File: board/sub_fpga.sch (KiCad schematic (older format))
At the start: 3 parts, among them U201 XC3S200-TQ144

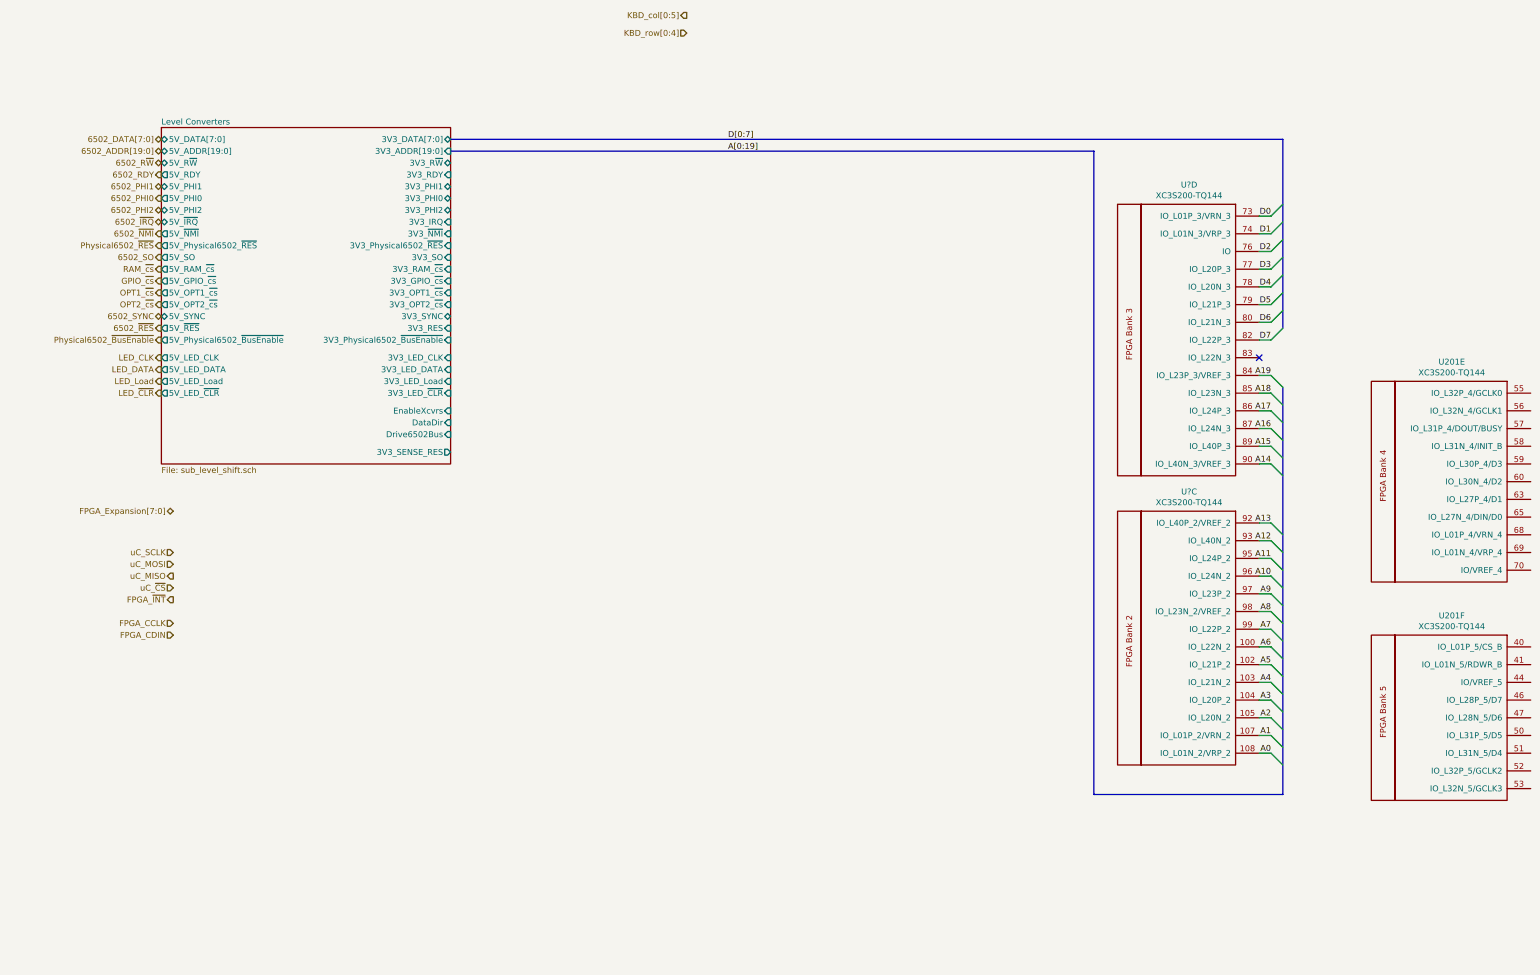
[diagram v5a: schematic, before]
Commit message: Bus signal connectivity rebuilt
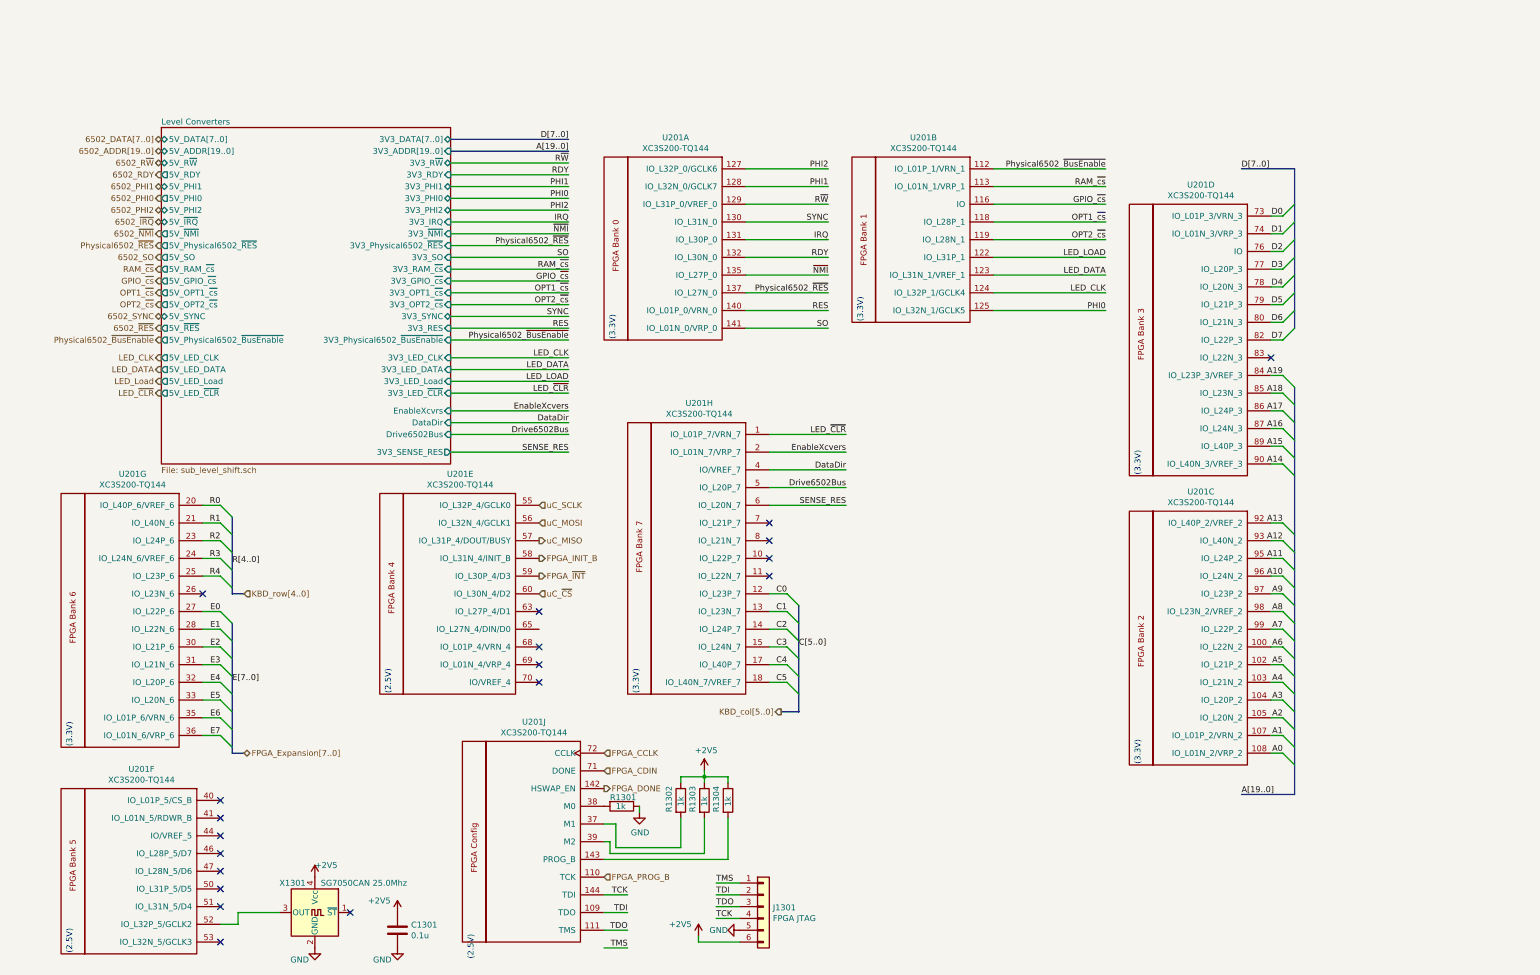
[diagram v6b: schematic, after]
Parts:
- added C1301: 0.1u, symbol Device:C
- added J1301: FPGA JTAG, symbol Connector_Generic:Conn_01x06
- added R1301, R1302, R1303, R1304: 1k, symbol Device:R
- added unit 2 of U201
- added unit 1 of U201
- added unit 8 of U201
- added unit 10 of U201
- added unit 7 of U201
- added X1301: SG7050CAN 25.0Mhz, Oscillator:Oscillator_SMD_SeikoEpson_SG8002CA-4Pin_7.0x5.0mm, symbol Oscillator:SG-211
- gave numbers to parts that had none: 1
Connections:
- net FPGA_CCLK: now also U201.72 (CCLK)
- net FPGA_CDIN: now also U201.71 (DONE)
- net FPGA_~INT: now also U201.59 (IO_L30P_4/D3)
- net GPIO_~cs: now also U201.116 (IO)
- net LED_CLK: now also U201.124 (IO_L32P_1/GCLK4)
- net LED_DATA: now also U201.123 (IO_L31N_1/VREF_1)
- net LED_~CLR: now also U201.1 (IO_L01P_7/VRN_7)
- net OPT1_~cs: now also U201.118 (IO_L28P_1)
- net OPT2_~cs: now also U201.119 (IO_L28N_1)
- net Physical6502_~BusEnable: now also U201.112 (IO_L01P_1/VRN_1)
- net Physical6502_~RES: now also U201.137 (IO_L27N_0)
- net RAM_~cs: now also U201.113 (IO_L01N_1/VRP_1)
- net uC_MISO: now also U201.57 (IO_L31P_4/DOUT/BUSY)
- net uC_MOSI: now also U201.56 (IO_L32N_4/GCLK1)
- net uC_SCLK: now also U201.55 (IO_L32P_4/GCLK0)
- net uC_~CS: now also U201.60 (IO_L30N_4/D2)
- net FPGA_INIT_B: now reaches U201.58 (IO_L31N_4/INIT_B)
- net at U201.52 (IO_L32P_5/GCLK2): now also X1301.3 (OUT)
- new net: R1304.2, U201.143 (PROG_B)
- new net: R1302.2, U201.37 (M1)
- new net: R1301.2, U201.38 (M0)
- new net: R1303.2, U201.39 (M2)
- new net +2V5: C1301.1, J1301.6 (Pin_6), R1302.1, R1303.1, R1304.1, X1301.4 (Vcc)
- new net C0: U201.12 (IO_L23P_7)
- new net C1: U201.13 (IO_L23N_7)
- new net C2: U201.14 (IO_L24P_7)
- new net C3: U201.15 (IO_L24N_7)
- new net C4: U201.17 (IO_L40P_7)
- new net C5: U201.18 (IO_L40N_7/VREF_7)
- new net DataDir: U201.4 (IO/VREF_7)
- new net Drive6502Bus: U201.5 (IO_L20P_7)
- new net E0: U201.27 (IO_L22P_6)
- new net E1: U201.28 (IO_L22N_6)
- new net E2: U201.30 (IO_L21P_6)
- new net E3: U201.31 (IO_L21N_6)
- new net E4: U201.32 (IO_L20P_6)
- new net E5: U201.33 (IO_L20N_6)
- new net E6: U201.35 (IO_L01P_6/VRN_6)
- new net E7: U201.36 (IO_L01N_6/VRP_6)
- new net EnableXcvers: U201.2 (IO_L01N_7/VRP_7)
- new net FPGA_DONE: U201.142 (HSWAP_EN)
- new net FPGA_PROG_B: U201.110 (TCK)
- new net GND: C1301.2, J1301.5 (Pin_5), R1301.1, X1301.2 (GND)
- new net IRQ: U201.131 (IO_L30P_0)
- new net LED_LOAD: U201.122 (IO_L31P_1)
- new net PHI0: U201.125 (IO_L32N_1/GCLK5)
- new net PHI1: U201.128 (IO_L32N_0/GCLK7)
- new net PHI2: U201.127 (IO_L32P_0/GCLK6)
- new net R0: U201.20 (IO_L40P_6/VREF_6)
- new net R1: U201.21 (IO_L40N_6)
- new net R2: U201.23 (IO_L24P_6)
- new net R3: U201.24 (IO_L24N_6/VREF_6)
- new net R4: U201.25 (IO_L23P_6)
- new net RDY: U201.132 (IO_L30N_0)
- new net RES: U201.140 (IO_L01P_0/VRN_0)
- new net R~W: U201.129 (IO_L31P_0/VREF_0)
- new net SENSE_RES: U201.6 (IO_L20N_7)
- new net SO: U201.141 (IO_L01N_0/VRP_0)
- new net SYNC: U201.130 (IO_L31N_0)
- new net TCK: J1301.4 (Pin_4), U201.144 (TDI)
- new net TDI: J1301.2 (Pin_2), U201.109 (TDO)
- new net TDO: J1301.3 (Pin_3), U201.111 (TMS)
- new net TMS: J1301.1 (Pin_1)
- new net ~NMI: U201.135 (IO_L27P_0)
- no-connect marks 1 -> 19
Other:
- note added: "(2.5V)"
- note added: "(3.3V)"
- moved on the sheet: U201C, U201D, U201E, U201F

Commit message: gpio done
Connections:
- net FPGA_~INT: now also U201.60 (IO_L30N_4/D2); no longer U201.59 (IO_L30P_4/D3)
- net uC_MISO: now also U201.59 (IO_L30P_4/D3); no longer U201.57 (IO_L31P_4/DOUT/BUSY)
- net uC_MOSI: now also U201.57 (IO_L31P_4/DOUT/BUSY); no longer U201.56 (IO_L32N_4/GCLK1)
- net uC_SCLK: now also U201.56 (IO_L32N_4/GCLK1); no longer U201.55 (IO_L32P_4/GCLK0)
- net uC_~CS: now also U201.63 (IO_L27P_4/D1); no longer U201.60 (IO_L30N_4/D2)
- net G7: now reaches U201.40 (IO_L01P_5/CS_B)
- net G6: now reaches U201.41 (IO_L01N_5/RDWR_B)
- net G5: now reaches U201.44 (IO/VREF_5)
- net G4: now reaches U201.46 (IO_L28P_5/D7)
- net G3: now reaches U201.47 (IO_L28N_5/D6)
- net G2: now reaches U201.50 (IO_L31P_5/D5)
- net G1: now reaches U201.51 (IO_L31N_5/D4)
- net at X1301.3 (OUT): now also U201.53 (IO_L32N_5/GCLK3); no longer U201.52 (IO_L32P_5/GCLK2)
- net GPIO_~cs: no longer names the net of U201.116 (IO)
- new net G0: U201.52 (IO_L32P_5/GCLK2)
- new net GPIO_R~W: U201.55 (IO_L32P_4/GCLK0)
- no-connect marks 19 -> 11

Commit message: Schematics mostly complete
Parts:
- added Q1301: Q_NPN_BEC, symbol Device:Q_NPN_BEC
- added R1305: 1k, symbol Device:R
- added R1306: 68, symbol Device:R
- R1301, R1304: value 1k -> 4.7k
- R1302: value 1k -> 330
- R1303: value 1k -> 68
- renumbered U201 to U205
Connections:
- net +2V5: now also R1302.2, U205.37 (M1), U205.38 (M0), U205.39 (M2); no longer C1301.1, R1302.1, R1303.1, R1304.1, X1301.4 (Vcc)
- net FPGA_CCLK: now also R1303.1; no longer U205.72 (CCLK)
- net FPGA_CDIN: now also U205.65 (IO_L27N_4/DIN/D0); no longer U205.71 (DONE)
- net FPGA_DONE: now also R1304.2, Q1301.3 (C); no longer U205.142 (HSWAP_EN)
- net FPGA_INIT_B: now also R1301.2
- net FPGA_PROG_B: now also R1306.1; no longer U205.110 (TCK)
- net GND: now also U205.142 (HSWAP_EN), Q1301.2 (E); no longer R1301.1
- net TCK: now also U205.110 (TCK); no longer U205.144 (TDI)
- net TDI: now also U205.144 (TDI); no longer U205.109 (TDO)
- net TDO: now also U205.109 (TDO); no longer U205.111 (TMS)
- net TMS: now also U205.111 (TMS)
- net at U205.143 (PROG_B): now also R1306.2; no longer R1304.2
- net at R1303.2: now also U205.72 (CCLK); no longer U205.39 (M2)
- new net: R1302.1, R1305.2, U205.71 (DONE)
- new net: Q1301.1 (B), R1305.1
- new net +3V3: C1301.1, R1301.1, R1304.1, X1301.4 (Vcc)
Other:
- moved on the sheet: C1301, J1301, U205E, U205H, U205J
